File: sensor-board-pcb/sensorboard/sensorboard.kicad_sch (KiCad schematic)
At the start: 19 parts, among them J1 TO_MOTHERBOARD, J10 PZT_08, J11 PZT_09, J12 PZT_10, J13 PZT_11, J14 PZT_12, J15 PZT_13, J16 PZT_14, J17 PZT_15, J2 PZT_00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

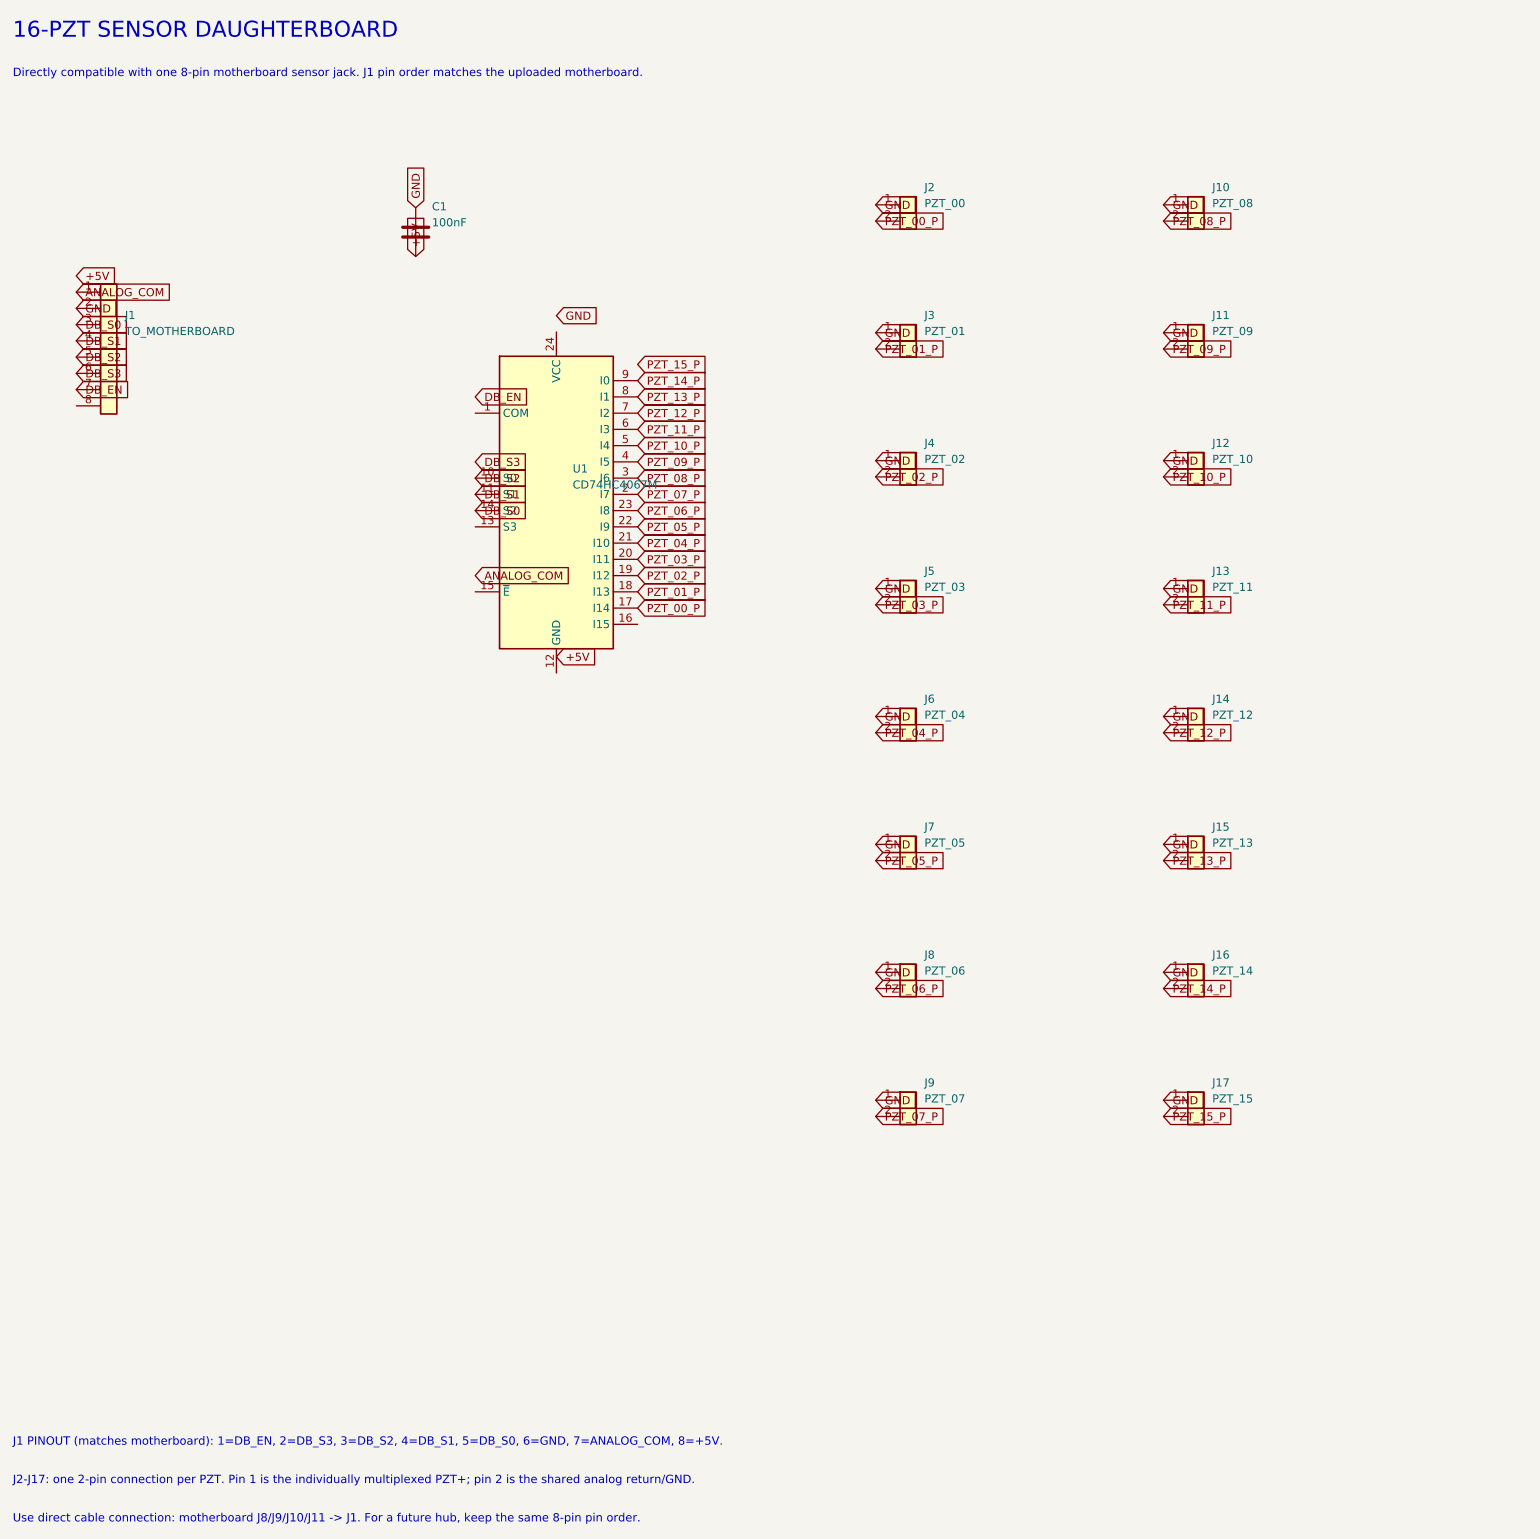
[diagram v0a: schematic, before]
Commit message: fixed erc and drc issues, fixing routing
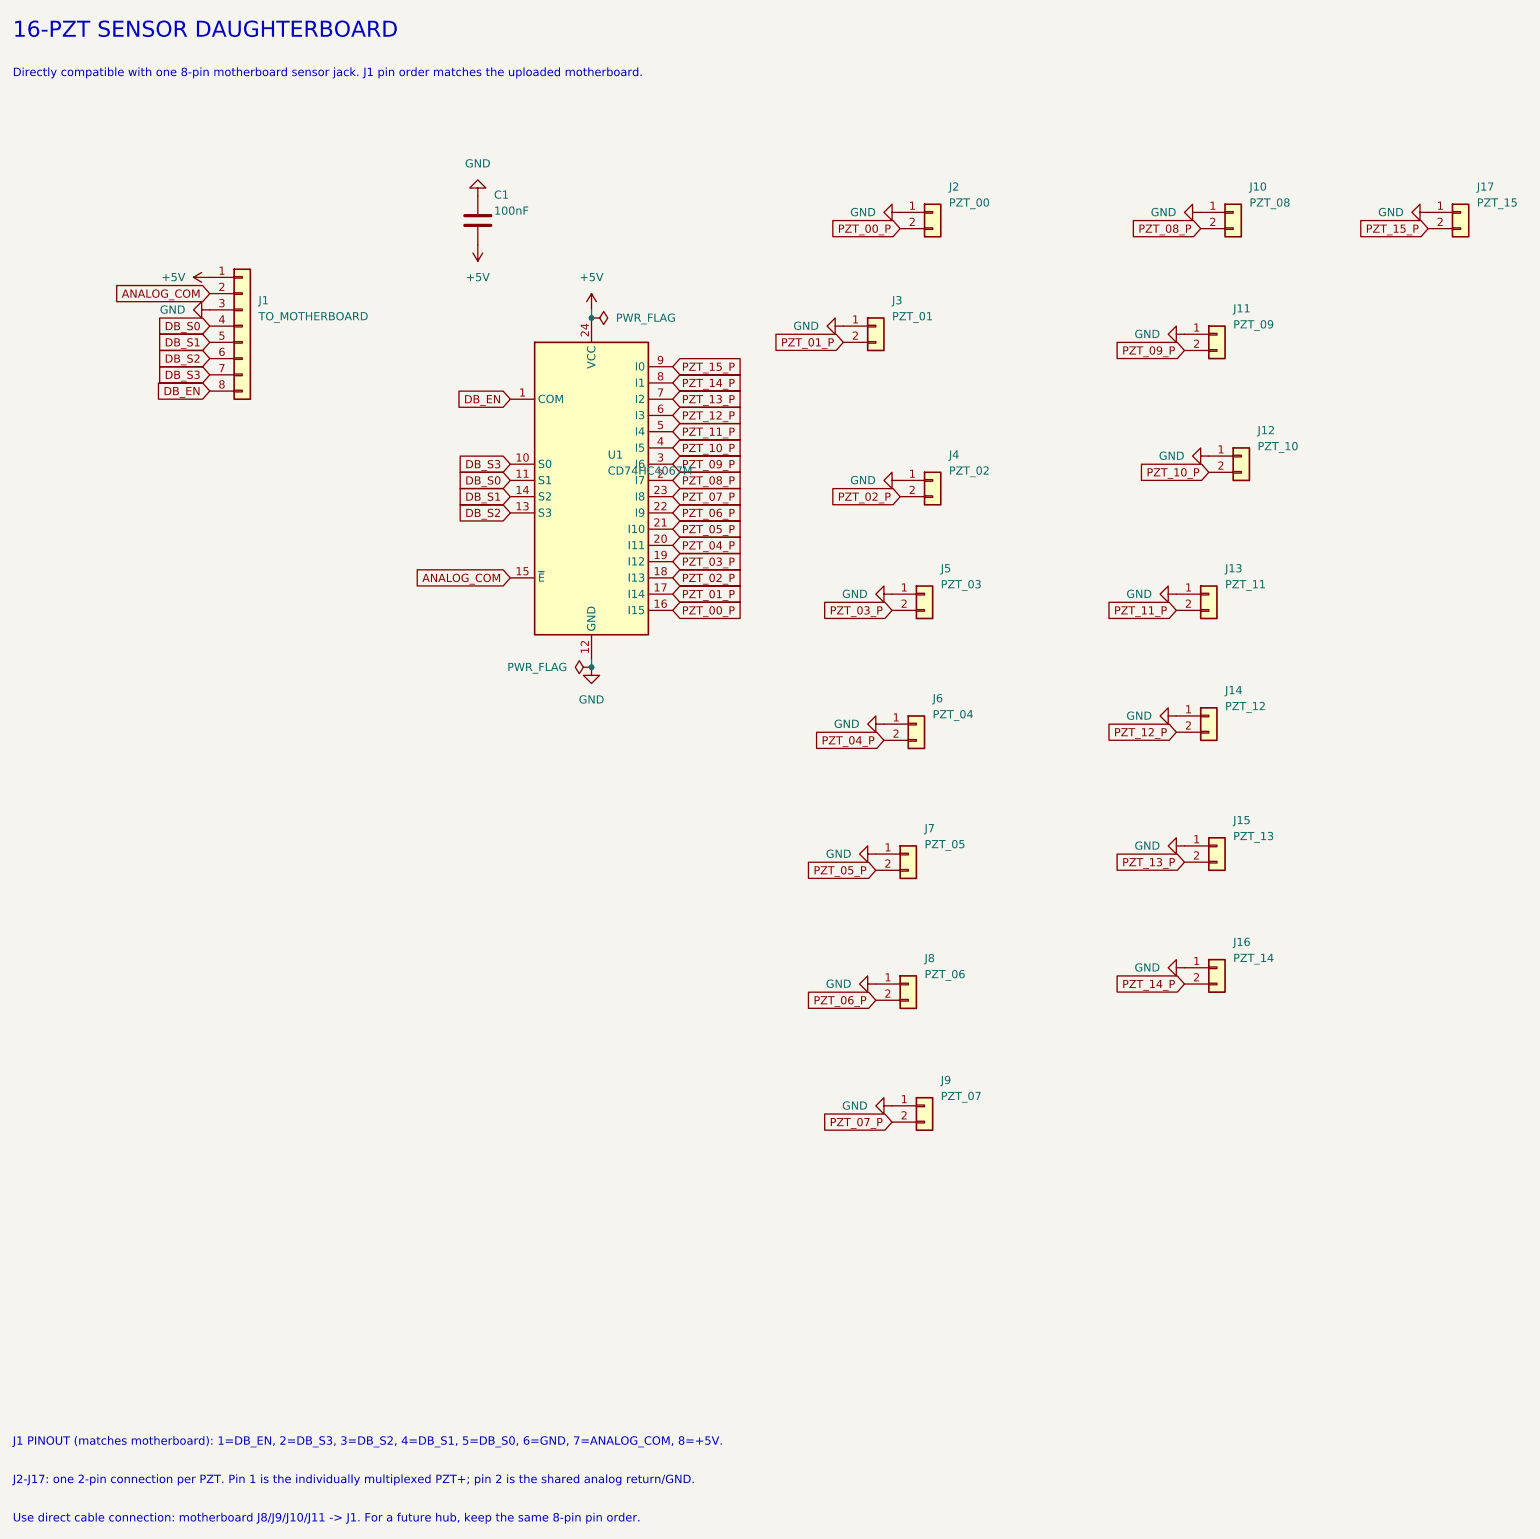
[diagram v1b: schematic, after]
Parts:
- U1: footprint Package_SO:SOIC-24W_7.5x15.4mm_P1.27mm -> Package_DIP:DIP-24_W7.62mm
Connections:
- net +5V: now also J1.1 (Pin_1), U1.24 (VCC)
- net ANALOG_COM: now also J1.2 (Pin_2), U1.15 (~{E}); no longer J1.1 (Pin_1)
- net DB_EN: now also J1.8 (Pin_8), U1.1 (COM); no longer J1.7 (Pin_7)
- net DB_S0: now also J1.4 (Pin_4), U1.11 (S1); no longer J1.3 (Pin_3), U1.14 (S2)
- net DB_S1: now also J1.5 (Pin_5), U1.14 (S2); no longer J1.4 (Pin_4), U1.11 (S1)
- net DB_S2: now also J1.6 (Pin_6), U1.13 (S3); no longer J1.5 (Pin_5), U1.10 (S0)
- net DB_S3: now also J1.7 (Pin_7), U1.10 (S0); no longer J1.6 (Pin_6)
- net GND: now also J1.3 (Pin_3), U1.12 (GND); no longer J1.2 (Pin_2)
- net PZT_00_P: now also U1.16 (I15); no longer U1.17 (I14)
- net PZT_01_P: now also U1.17 (I14); no longer U1.18 (I13)
- net PZT_02_P: now also U1.18 (I13); no longer U1.19 (I12)
- net PZT_03_P: now also U1.19 (I12); no longer U1.20 (I11)
- net PZT_04_P: now also U1.20 (I11); no longer U1.21 (I10)
- net PZT_05_P: now also U1.21 (I10); no longer U1.22 (I9)
- net PZT_06_P: now also U1.22 (I9); no longer U1.23 (I8)
- net PZT_07_P: now also U1.23 (I8); no longer U1.2 (I7)
- net PZT_08_P: now also U1.2 (I7); no longer U1.3 (I6)
- net PZT_09_P: now also U1.3 (I6); no longer U1.4 (I5)
- net PZT_10_P: now also U1.4 (I5); no longer U1.5 (I4)
- net PZT_11_P: now also U1.5 (I4); no longer U1.6 (I3)
- net PZT_12_P: now also U1.6 (I3); no longer U1.7 (I2)
- net PZT_13_P: now also U1.7 (I2); no longer U1.8 (I1)
- net PZT_14_P: now also U1.8 (I1); no longer U1.9 (I0)
- net PZT_15_P: now also U1.9 (I0)
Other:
- moved on the sheet: C1, U1
